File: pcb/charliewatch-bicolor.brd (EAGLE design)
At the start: 85.1 x 54.9 mm, 79 parts, among them U2 CC430F5137IRGZR, X1 CRYSTALS-NOGND-IQXC-25

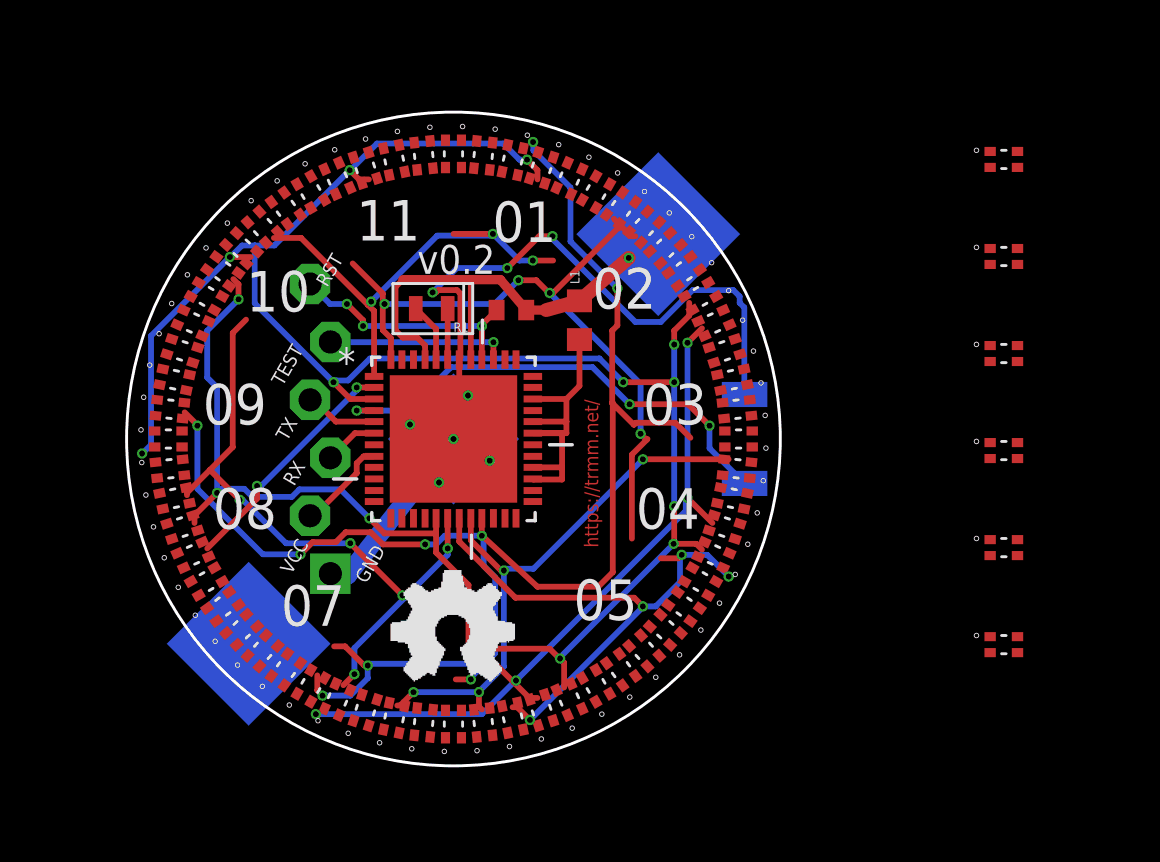
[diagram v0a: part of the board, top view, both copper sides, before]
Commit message: initial positioning for the bicolor leds
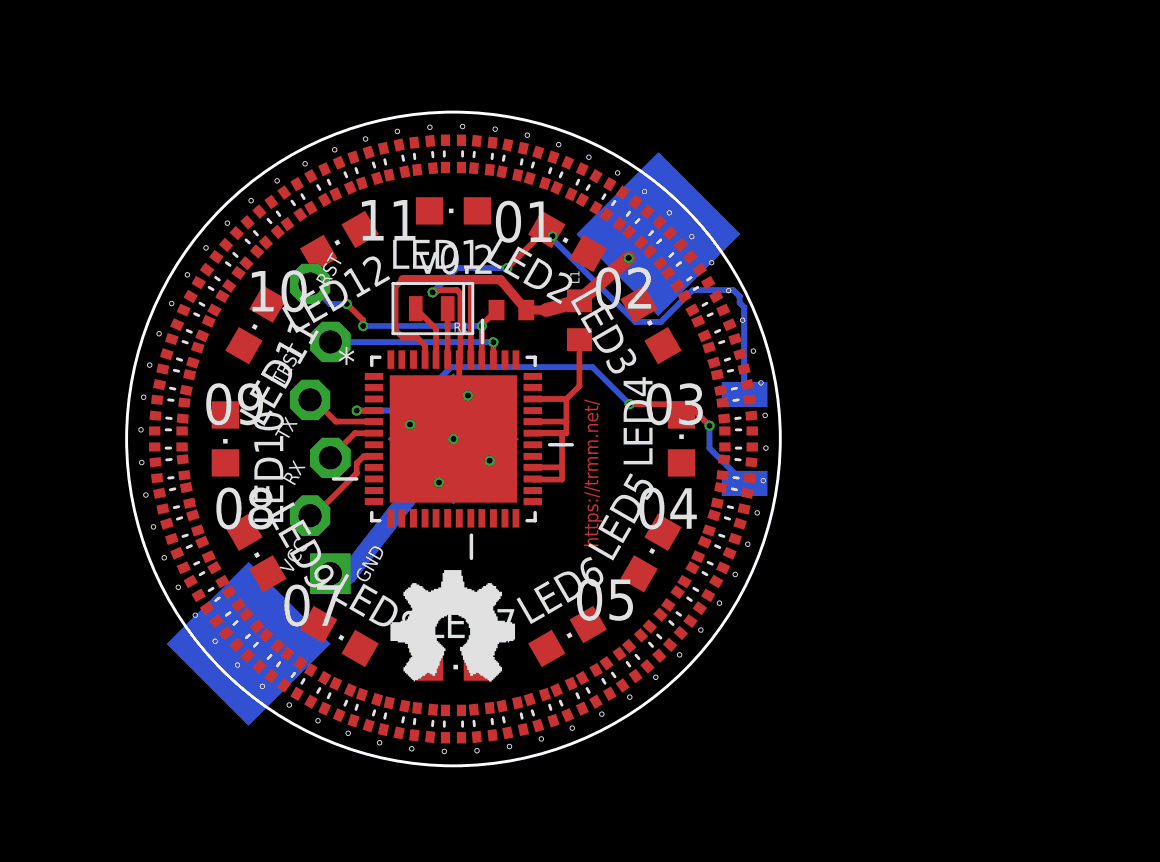
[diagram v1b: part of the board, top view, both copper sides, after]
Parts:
- removed D61, D62, D63, D64, D65, D66: APHB1608SYKSURKC, APHB1608SYKSURKC:LED_APHB1608SYKSURKC
- added LED1, LED10, LED11, LED12, LED2, LED3, LED4, LED5, LED6, LED7, LED8, LED9: (no value), led:CHIPLED_0805
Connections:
- removed net N$1: D1.2, D1.3, D10.2, D10.3, D13.2, D13.3, D17.2, D17.3, D2.2, D2.3, D21.2, D21.3, D26.2, D26.3, D3.2, D3.3, D31.2, D31.3, D5.2, D5.3, D7.2, D7.3
- removed net N$10: D21.1, D21.4, D27.1, D27.4, D33.1, D33.4, D39.1, D39.4, D44.1, D44.4, D49.1, D49.4, D53.1, D53.4, D57.1, D57.4, D60.1, D60.4, D64.2, D64.3, D65.2, D65.3
- removed net N$11: D26.1, D26.4, D32.1, D32.4, D38.1, D38.4, D43.1, D43.4, D48.1, D48.4, D52.1, D52.4, D56.1, D56.4, D59.1, D59.4, D62.1, D62.4, D64.1, D64.4, D66.2, D66.3
- removed net N$12: D31.1, D31.4, D37.1, D37.4, D42.1, D42.4, D47.1, D47.4, D51.1, D51.4, D55.1, D55.4, D58.1, D58.4, D61.1, D61.4, D63.1, D63.4, D65.1, D65.4, D66.1, D66.4
- removed net N$2: D1.1, D1.4, D11.2, D11.3, D14.2, D14.3, D18.2, D18.3, D22.2, D22.3, D27.2, D27.3, D32.2, D32.3, D37.2, D37.3, D4.2, D4.3, D6.2, D6.3, D8.2, D8.3
- removed net N$3: D12.2, D12.3, D15.2, D15.3, D19.2, D19.3, D2.1, D2.4, D23.2, D23.3, D28.2, D28.3, D33.2, D33.3, D38.2, D38.3, D4.1, D4.4, D42.2, D42.3, D9.2, D9.3
- removed net N$4: D16.2, D16.3, D20.2, D20.3, D24.2, D24.3, D29.2, D29.3, D3.1, D3.4, D34.2, D34.3, D39.2, D39.3, D43.2, D43.3, D47.2, D47.3, D6.1, D6.4, D9.1, D9.4
- removed net N$5: D12.1, D12.4, D16.1, D16.4, D25.2, D25.3, D30.2, D30.3, D35.2, D35.3, D40.2, D40.3, D44.2, D44.3, D48.2, D48.3, D5.1, D5.4, D51.2, D51.3, D8.1, D8.4
- removed net N$6: D11.1, D11.4, D15.1, D15.4, D20.1, D20.4, D25.1, D25.4, D36.2, D36.3, D41.2, D41.3, D45.2, D45.3, D49.2, D49.3, D52.2, D52.3, D55.2, D55.3, D7.1, D7.4
- removed net N$7: D10.1, D10.4, D14.1, D14.4, D19.1, D19.4, D24.1, D24.4, D30.1, D30.4, D36.1, D36.4, D46.2, D46.3, D50.2, D50.3, D53.2, D53.3, D56.2, D56.3, D58.2, D58.3
- removed net N$8: D13.1, D13.4, D18.1, D18.4, D23.1, D23.4, D29.1, D29.4, D35.1, D35.4, D41.1, D41.4, D46.1, D46.4, D54.2, D57.2, D57.3, D59.2, D59.3, D61.2, D61.3
- removed net N$9: D17.1, D17.4, D22.1, D22.4, D28.1, D28.4, D34.1, D34.4, D40.1, D40.4, D45.1, D45.4, D50.1, D50.4, D54.1, D54.4, D60.2, D60.3, D62.2, D62.3, D63.2, D63.3
- removed net P3.5: U2.16
- removed net P3.6: U2.15
- removed net P3.7: U2.14
- new net B10: D26.1, D26.4, D32.1, D32.4, D38.1, D38.4, D43.1, D43.4, D48.1, D48.4, D52.1, D52.4, D55.1, D55.4, D56.1, D56.4, D58.1, D58.4, D59.1, D59.4, LED7.A, U2.1
- new net B11: D31.1, D31.4, D37.1, D37.4, D42.1, D42.4, D47.1, D47.4, D51.1, D51.4, LED1.A, LED2.A, LED3.A, LED4.A, LED5.A, LED6.A, U2.48
- new net B9: D21.1, D21.4, D27.1, D27.4, D33.1, D33.4, D39.1, D39.4, D44.1, D44.4, D49.1, D49.4, D53.1, D53.4, D57.1, D57.4, D58.2, D58.3, D60.1, D60.4, LED8.A, U2.2
- net B0: now also D1.2, D1.3, D10.2, D10.3, D13.2, D13.3, D17.2, D17.3, D2.2, D2.3, D21.2, D21.3, D26.2, D26.3, D3.2, D3.3, D31.2, D31.3, D5.2, D5.3, D7.2, D7.3
- net B1: now also D1.1, D1.4, D11.2, D11.3, D14.2, D14.3, D18.2, D18.3, D22.2, D22.3, D27.2, D27.3, D32.2, D32.3, D37.2, D37.3, D4.2, D4.3, D6.2, D6.3, D8.2, D8.3
- net B2: now also D12.2, D12.3, D15.2, D15.3, D19.2, D19.3, D2.1, D2.4, D23.2, D23.3, D28.2, D28.3, D33.2, D33.3, D38.2, D38.3, D4.1, D4.4, D42.2, D42.3, D9.2, D9.3
- net B3: now also D16.2, D16.3, D20.2, D20.3, D24.2, D24.3, D29.2, D29.3, D3.1, D3.4, D34.2, D34.3, D39.2, D39.3, D43.2, D43.3, D47.2, D47.3, D6.1, D6.4, D9.1, D9.4
- net B4: now also D12.1, D12.4, D16.1, D16.4, D25.2, D25.3, D30.2, D30.3, D35.2, D35.3, D40.2, D40.3, D44.2, D44.3, D48.2, D48.3, D5.1, D5.4, D51.2, D51.3, D8.1, D8.4
- net B5: now also D11.1, D11.4, D15.1, D15.4, D20.1, D20.4, D25.1, D25.4, D36.2, D36.3, D41.2, D41.3, D45.2, D45.3, D49.2, D49.3, D52.2, D52.3, D7.1, D7.4, LED1.C, LED12.A, U2.16; no longer U2.3
- net B6: now also D10.1, D10.4, D14.1, D14.4, D19.1, D19.4, D24.1, D24.4, D30.1, D30.4, D36.1, D36.4, D46.2, D46.3, D50.2, D50.3, D53.2, D53.3, D56.2, D56.3, LED11.A, LED2.C, U2.15; no longer U2.2
- net B7: now also D13.1, D13.4, D18.1, D18.4, D23.1, D23.4, D29.1, D29.4, D35.1, D35.4, D41.1, D41.4, D46.1, D46.4, D54.2, D57.2, D57.3, D59.2, D59.3, LED10.A, U2.14; no longer U2.1
- net B8: now also D17.1, D17.4, D22.1, D22.4, D28.1, D28.4, D34.1, D34.4, D40.1, D40.4, D45.1, D45.4, D50.1, D50.4, D54.1, D54.4, D55.2, D55.3, D60.2, D60.3, LED9.A, U2.3; no longer U2.48
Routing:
- net B5: track 89.1 -> 0.00 mm, vias 14 -> 0
- net B4: track 62.8 -> 0.00 mm, vias 7 -> 0
- net B0: track 57.9 -> 0.00 mm, vias 7 -> 0
- net B8: track 31.3 -> 0.00 mm, vias 4 -> 0
- net B3: track 28.9 -> 0.00 mm, vias 5 -> 0
- net B1: track 25.2 -> 0.00 mm, vias 4 -> 0
- net B2: track 25.0 -> 0.00 mm, vias 4 -> 0
- net B7: track 20.2 -> 0.00 mm, vias 3 -> 0
- net B6: track 10.6 -> 0.00 mm, vias 2 -> 0

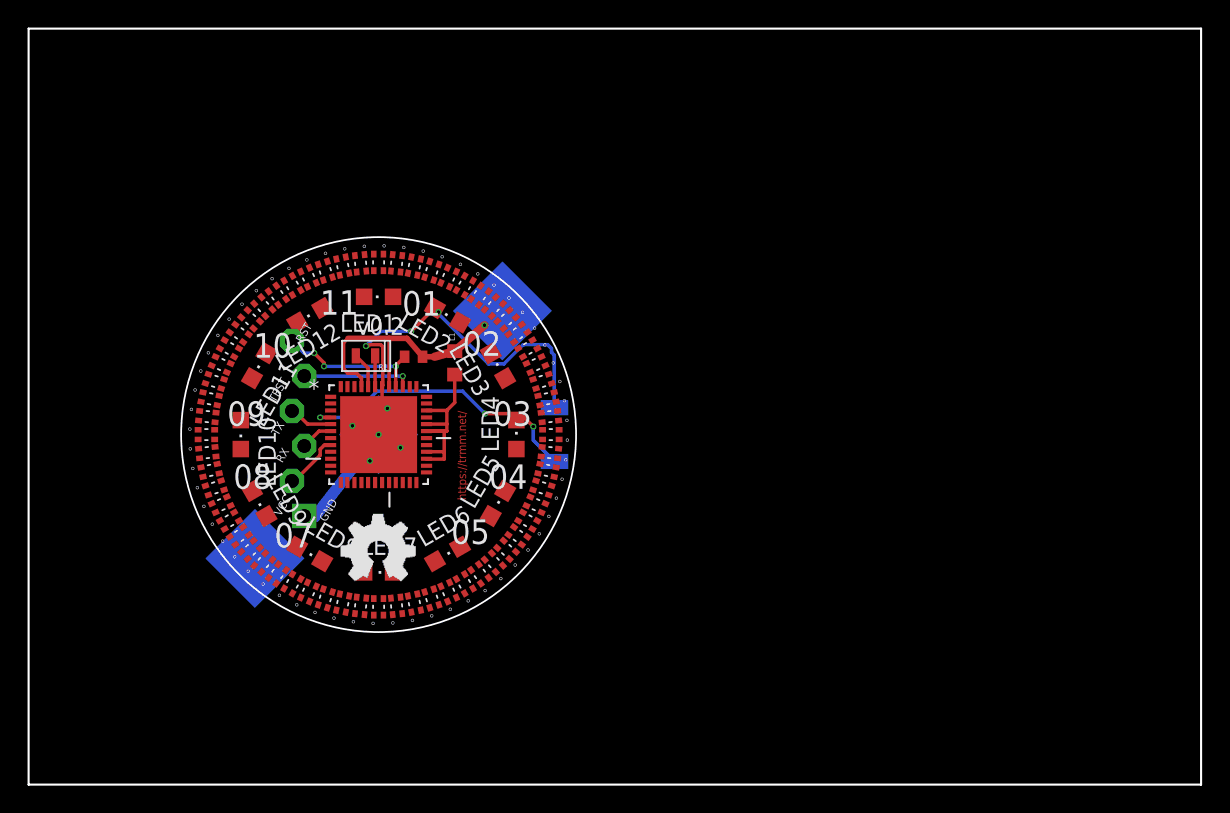
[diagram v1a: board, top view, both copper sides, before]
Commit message: change to through-hole cr2032 and hack up the layout
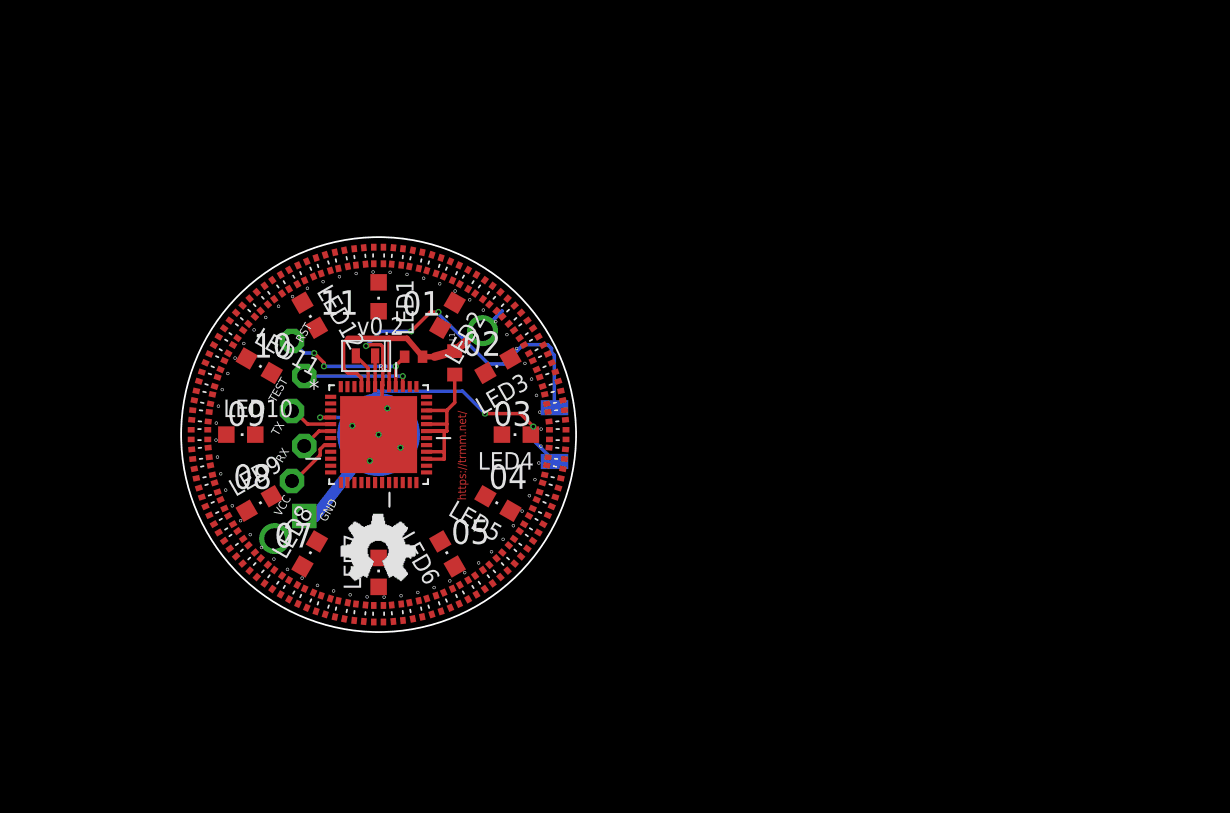
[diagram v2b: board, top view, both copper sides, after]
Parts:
- U$1: device adafruit:CR2032-SMD -> adafruit:CR2032-THRU
- moved D31 22.1 mm to (36.7, 31.9), turned to 30 degrees
- moved D37 19.0 mm to (36.7, 18.9), turned to 330 degrees
- moved D26 19.0 mm to (35.9, 33.0), turned to 36 degrees
- moved D16 18.0 mm to (25.4, 12.4), turned to 270 degrees
- moved D25 17.1 mm to (15.7, 16.7), turned to 222 degrees
- moved D9 16.1 mm to (35.9, 17.8), turned to 324 degrees
- moved D21 15.0 mm to (35.1, 34.1), turned to 42 degrees
- moved D42 15.0 mm to (26.8, 12.5), turned to 276 degrees
- moved D20 15.0 mm to (24.0, 12.5), turned to 264 degrees
- moved D32 15.0 mm to (37.3, 20.1), turned to 336 degrees
- moved D12 13.9 mm to (35.1, 16.7), turned to 318 degrees
- moved D30 12.8 mm to (14.9, 17.8), turned to 216 degrees
- moved D36 12.8 mm to (12.4, 25.4), turned to 180 degrees
- moved D24 11.6 mm to (22.7, 12.7), turned to 258 degrees
- moved D38 11.6 mm to (28.1, 12.7), turned to 282 degrees
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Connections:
- net VCC: now also U$1.+1; no longer U$1.+$1
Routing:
- net VCC: track 21.1 -> 23.1 mm
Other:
- board size 85.1 x 54.9 mm -> 28.7 x 28.7 mm
